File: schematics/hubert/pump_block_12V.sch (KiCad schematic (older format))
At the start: 14 parts, among them M1 PUMP12V, M2 PUMP12V, U2 L6205N

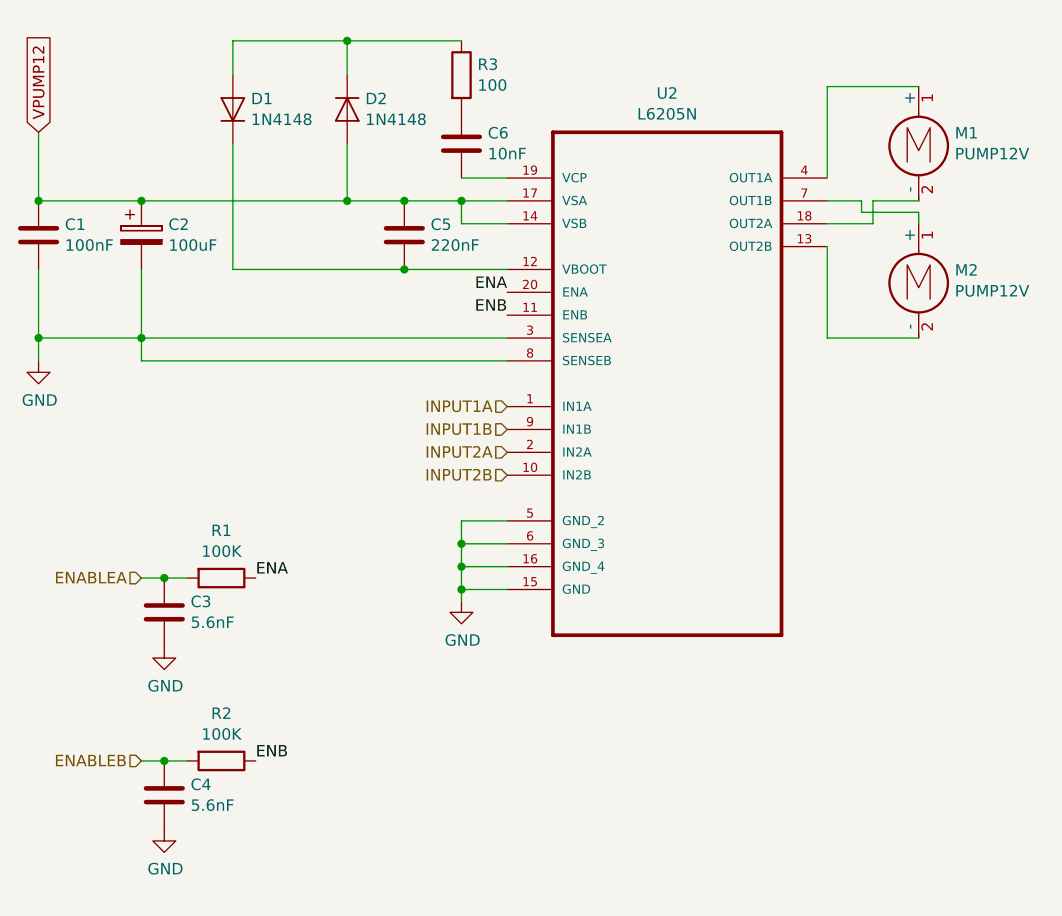
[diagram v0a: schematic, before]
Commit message: updated schematics
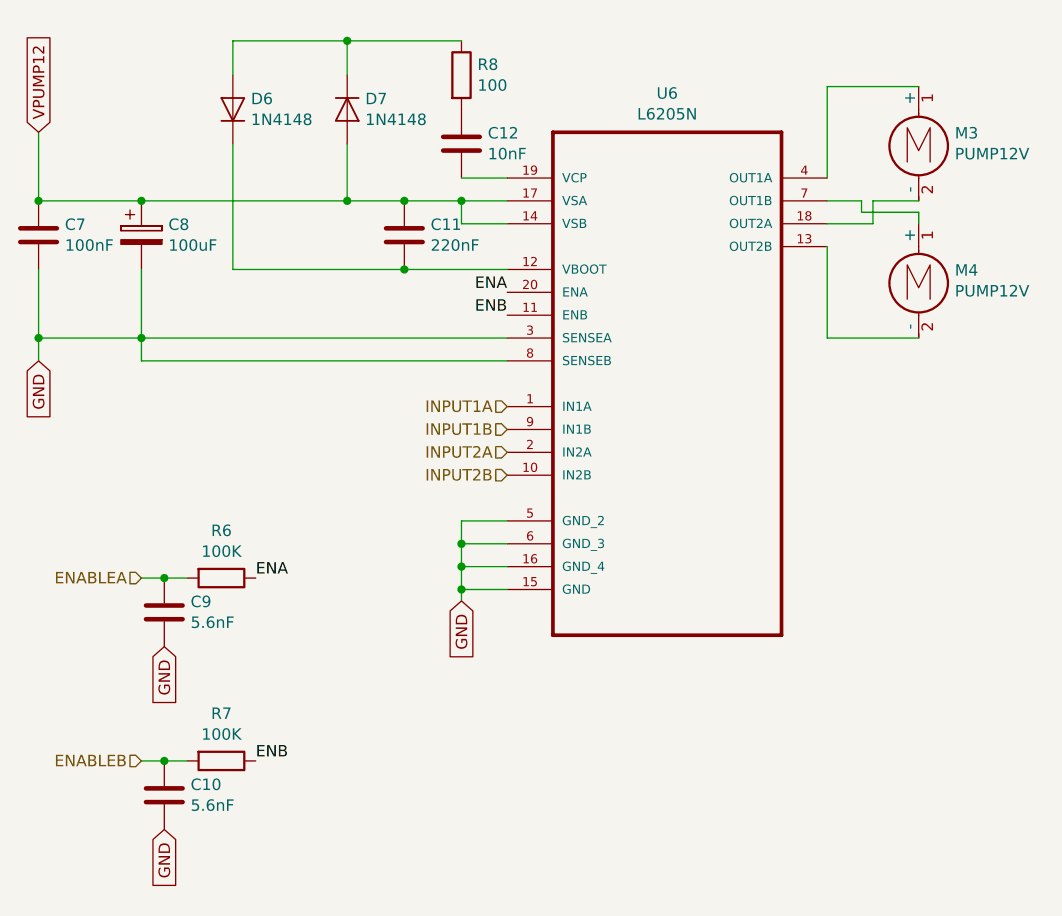
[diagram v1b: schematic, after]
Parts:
- renumbered D1 to D4, D2 to D5, R1 to R3, R2 to R4, R3 to R5, U2 to U5
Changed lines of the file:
@@
 $Descr A4 11693 8268
 encoding utf-8
-Sheet 2 6
+Sheet 3 7
 Title "Hubert"
-Date "2018-10-31"
-Rev "1"
+Date "2018-11-02"
+Rev "1.1"
 Comp ""
 Comment1 ""
@@
 P 6800 3100
 AR Path="/5BDAA834" Ref="U?"  Part="1"
-AR Path="/5BDA8753/5BDAA834" Ref="U2"  Part="1"
-AR Path="/5BDAC3DF/5BDAA834" Ref="U3"  Part="1"
-F 0 "U2" H 6800 4270 50  0000 C CNN
+AR Path="/5BDA8753/5BDAA834" Ref="U5"  Part="1"
+AR Path="/5BDAC3DF/5BDAA834" Ref="U6"  Part="1"
+F 0 "U6" H 6800 4270 50  0000 C CNN
 F 1 "L6205N" H 6800 4179 50  0000 C CNN
 F 2 "DIP254P762X510-20" H 6800 3100 50  0001 L BNN
@@
 	1    0    0    -1
 $EndComp
-$Comp
-L power:GND #PWR?
-U 1 1 5BDAA83B
-P 5900 4150
-AR Path="/5BDAA83B" Ref="#PWR?"  Part="1"
-AR Path="/5BDA8753/5BDAA83B" Ref="#PWR05"  Part="1"
-AR Path="/5BDAC3DF/5BDAA83B" Ref="#PWR010"  Part="1"
-F 0 "#PWR05" H 5900 3900 50  0001 C CNN
-F 1 "GND" H 5905 3977 50  0000 C CNN
-F 2 "" H 5900 4150 50  0001 C CNN
-F 3 "" H 5900 4150 50  0001 C CNN
-	1    5900 4150
-	1    0    0    -1
-$EndComp
 Wire Wire Line
 	5900 4150 5900 4100
@@
 P 5400 2000
 AR Path="/5BDB4D6F" Ref="D?"  Part="1"
-AR Path="/5BDA8753/5BDB4D6F" Ref="D2"  Part="1"
-AR Path="/5BDAC3DF/5BDB4D6F" Ref="D4"  Part="1"
-F 0 "D2" V 5354 2079 50  0000 L CNN
+AR Path="/5BDA8753/5BDB4D6F" Ref="D5"  Part="1"
+AR Path="/5BDAC3DF/5BDB4D6F" Ref="D7"  Part="1"
+F 0 "D7" V 5354 2079 50  0000 L CNN
 F 1 "1N4148" V 5445 2079 50  0000 L CNN
 F 2 "Diode_THT:D_DO-35_SOD27_P7.62mm_Horizontal" H 5400 1825 50  0001 C CNN
@@
 AR Path="/5BDA8753/5BDB4D70" Ref="C6"  Part="1"
 AR Path="/5BDAC3DF/5BDB4D70" Ref="C12"  Part="1"
-F 0 "C6" H 6015 2196 50  0000 L CNN
+F 0 "C12" H 6015 2196 50  0000 L CNN
 F 1 "10nF" H 6015 2105 50  0000 L CNN
 F 2 "" H 5938 2000 50  0001 C CNN
@@
 P 5900 1850
 AR Path="/5BDB4D71" Ref="R?"  Part="1"
-AR Path="/5BDA8753/5BDB4D71" Ref="R3"  Part="1"
-AR Path="/5BDAC3DF/5BDB4D71" Ref="R6"  Part="1"
-F 0 "R3" H 5970 1896 50  0000 L CNN
+AR Path="/5BDA8753/5BDB4D71" Ref="R5"  Part="1"
+AR Path="/5BDAC3DF/5BDB4D71" Ref="R8"  Part="1"
+F 0 "R8" H 5970 1896 50  0000 L CNN
 F 1 "100" H 5970 1805 50  0000 L CNN
 F 2 "" V 5830 1850 50  0001 C CNN
@@
 P 4900 2000
 AR Path="/5BDB4D72" Ref="D?"  Part="1"
-AR Path="/5BDA8753/5BDB4D72" Ref="D1"  Part="1"
-AR Path="/5BDAC3DF/5BDB4D72" Ref="D3"  Part="1"
-F 0 "D1" V 4946 1921 50  0000 R CNN
+AR Path="/5BDA8753/5BDB4D72" Ref="D4"  Part="1"
+AR Path="/5BDAC3DF/5BDB4D72" Ref="D6"  Part="1"
+F 0 "D6" V 4946 1921 50  0000 R CNN
 F 1 "1N4148" V 4855 1921 50  0000 R CNN
 F 2 "Diode_THT:D_DO-35_SOD27_P7.62mm_Horizontal" H 4900 1825 50  0001 C CNN
@@
 AR Path="/5BDA8753/5BDB4D73" Ref="C5"  Part="1"
 AR Path="/5BDAC3DF/5BDB4D73" Ref="C11"  Part="1"
-F 0 "C5" H 5765 2596 50  0000 L CNN
+F 0 "C11" H 5765 2596 50  0000 L CNN
 F 1 "220nF" H 5765 2505 50  0000 L CNN
 F 2 "" H 5688 2400 50  0001 C CNN
@@
 AR Path="/5BDA8753/5BDAA887" Ref="C2"  Part="1"
 AR Path="/5BDAC3DF/5BDAA887" Ref="C8"  Part="1"
-F 0 "C2" H 4618 2596 50  0000 L CNN
+F 0 "C8" H 4618 2596 50  0000 L CNN
 F 1 "100uF" H 4618 2505 50  0000 L CNN
 F 2 "" H 4538 2400 50  0001 C CNN
@@
 AR Path="/5BDA8753/5BDB4D75" Ref="C1"  Part="1"
 AR Path="/5BDAC3DF/5BDB4D75" Ref="C7"  Part="1"
-F 0 "C1" H 4165 2596 50  0000 L CNN
+F 0 "C7" H 4165 2596 50  0000 L CNN
 F 1 "100nF" H 4165 2505 50  0000 L CNN
 F 2 "" H 4088 2400 50  0001 C CNN
@@
 $EndComp
 Connection ~ 4050 2400
-$Comp
-L power:GND #PWR?
-U 1 1 5BDB4D76
-P 4050 3100
-AR Path="/5BDB4D76" Ref="#PWR?"  Part="1"
-AR Path="/5BDA8753/5BDB4D76" Ref="#PWR02"  Part="1"
-AR Path="/5BDAC3DF/5BDB4D76" Ref="#PWR07"  Part="1"
-F 0 "#PWR02" H 4050 2850 50  0001 C CNN
-F 1 "GND" H 4055 2927 50  0000 C CNN
-F 2 "" H 4050 3100 50  0001 C CNN
-F 3 "" H 4050 3100 50  0001 C CNN
-	1    4050 3100
-	1    0    0    -1
-$EndComp
 Wire Wire Line
 	4050 2700 4050 3000
@@
 AR Path="/5BDA8753/5BDAA8AA" Ref="C3"  Part="1"
 AR Path="/5BDAC3DF/5BDAA8AA" Ref="C9"  Part="1"
-F 0 "C3" H 4715 4246 50  0000 L CNN
+F 0 "C9" H 4715 4246 50  0000 L CNN
 F 1 "5.6nF" H 4715 4155 50  0000 L CNN
 F 2 "" H 4638 4050 50  0001 C CNN
@@
 AR Path="/5BDA8753/5BDAA8B1" Ref="C4"  Part="1"
 AR Path="/5BDAC3DF/5BDAA8B1" Ref="C10"  Part="1"
-F 0 "C4" H 4715 5046 50  0000 L CNN
+F 0 "C10" H 4715 5046 50  0000 L CNN
 F 1 "5.6nF" H 4715 4955 50  0000 L CNN
 F 2 "" H 4638 4850 50  0001 C CNN
@@
 $EndComp
 $Comp
-L power:GND #PWR?
-U 1 1 5BDB4D78
-P 4600 4350
-AR Path="/5BDB4D78" Ref="#PWR?"  Part="1"
-AR Path="/5BDA8753/5BDB4D78" Ref="#PWR03"  Part="1"
-AR Path="/5BDAC3DF/5BDB4D78" Ref="#PWR08"  Part="1"
-F 0 "#PWR03" H 4600 4100 50  0001 C CNN
-F 1 "GND" H 4605 4177 50  0000 C CNN
-F 2 "" H 4600 4350 50  0001 C CNN
-F 3 "" H 4600 4350 50  0001 C CNN
-	1    4600 4350
-	1    0    0    -1
-$EndComp
-$Comp
-L power:GND #PWR?
-U 1 1 5BDAA8BE
-P 4600 5150
-AR Path="/5BDAA8BE" Ref="#PWR?"  Part="1"
-AR Path="/5BDA8753/5BDAA8BE" Ref="#PWR04"  Part="1"
-AR Path="/5BDAC3DF/5BDAA8BE" Ref="#PWR09"  Part="1"
-F 0 "#PWR04" H 4600 4900 50  0001 C CNN
-F 1 "GND" H 4605 4977 50  0000 C CNN
-F 2 "" H 4600 5150 50  0001 C CNN
-F 3 "" H 4600 5150 50  0001 C CNN
-	1    4600 5150
-	1    0    0    -1
-$EndComp
-$Comp
 L Device:R R?
 U 1 1 5BDB4D79
 P 4850 4050
 AR Path="/5BDB4D79" Ref="R?"  Part="1"
-AR Path="/5BDA8753/5BDB4D79" Ref="R1"  Part="1"
-AR Path="/5BDAC3DF/5BDB4D79" Ref="R4"  Part="1"
-F 0 "R1" V 4643 4050 50  0000 C CNN
+AR Path="/5BDA8753/5BDB4D79" Ref="R3"  Part="1"
+AR Path="/5BDAC3DF/5BDB4D79" Ref="R6"  Part="1"
+F 0 "R6" V 4643 4050 50  0000 C CNN
 F 1 "100K" V 4734 4050 50  0000 C CNN
 F 2 "" V 4780 4050 50  0001 C CNN
@@
 P 4850 4850
 AR Path="/5BDAA8CB" Ref="R?"  Part="1"
-AR Path="/5BDA8753/5BDAA8CB" Ref="R2"  Part="1"
-AR Path="/5BDAC3DF/5BDAA8CB" Ref="R5"  Part="1"
-F 0 "R2" V 4643 4850 50  0000 C CNN
+AR Path="/5BDA8753/5BDAA8CB" Ref="R4"  Part="1"
+AR Path="/5BDAC3DF/5BDAA8CB" Ref="R7"  Part="1"
+F 0 "R7" V 4643 4850 50  0000 C CNN
 F 1 "100K" V 4734 4850 50  0000 C CNN
 F 2 "" V 4780 4850 50  0001 C CNN
@@
 AR Path="/5BDA8753/5BDB4D7A" Ref="M1"  Part="1"
 AR Path="/5BDAC3DF/5BDB4D7A" Ref="M3"  Part="1"
-F 0 "M1" H 8058 2096 50  0000 L CNN
+F 0 "M3" H 8058 2096 50  0000 L CNN
 F 1 "PUMP12V" H 8058 2005 50  0000 L CNN
 F 2 "" H 7900 2010 50  0001 C CNN
@@
 AR Path="/5BDA8753/5BDAA8E9" Ref="M2"  Part="1"
 AR Path="/5BDAC3DF/5BDAA8E9" Ref="M4"  Part="1"
-F 0 "M2" H 8058 2696 50  0000 L CNN
+F 0 "M4" H 8058 2696 50  0000 L CNN
 F 1 "PUMP12V" H 8058 2605 50  0000 L CNN
 F 2 "" H 7900 2610 50  0001 C CNN
@@
 Text GLabel 4050 2100 1    50   Input ~ 0
 VPUMP12
+Text GLabel 4600 4350 3    50   Input ~ 0
+GND
+Text GLabel 4600 5150 3    50   Input ~ 0
+GND
+Text GLabel 4050 3100 3    50   Input ~ 0
+GND
+Text GLabel 5900 4150 3    50   Input ~ 0
+GND
 $EndSCHEMATC

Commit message: started working on layout
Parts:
- C1, C3, C4, C5, C6: footprint (none) -> Capacitor_THT:CP_Radial_D5.0mm_P2.50mm
- C2: footprint (none) -> Capacitor_THT:CP_Radial_D6.3mm_P2.50mm
- R3, R4, R5: footprint (none) -> Resistor_THT:R_Axial_DIN0617_L17.0mm_D6.0mm_P25.40mm_Horizontal
- U5: footprint DIP254P762X510-20 -> Package_DIP:DIP-20_W7.62mm_Socket
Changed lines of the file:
@@
 Sheet 3 7
 Title "Hubert"
-Date "2018-11-02"
-Rev "1.1"
+Date "2018-11-05"
+Rev "1.2"
 Comp ""
 Comment1 ""
@@
 AR Path="/5BDA8753/5BDAA834" Ref="U5"  Part="1"
 AR Path="/5BDAC3DF/5BDAA834" Ref="U6"  Part="1"
-F 0 "U6" H 6800 4270 50  0000 C CNN
+F 0 "U5" H 6800 4270 50  0000 C CNN
 F 1 "L6205N" H 6800 4179 50  0000 C CNN
-F 2 "DIP254P762X510-20" H 6800 3100 50  0001 L BNN
+F 2 "Package_DIP:DIP-20_W7.62mm_Socket" H 6800 3100 50  0001 L BNN
 F 3 "L6205N" H 6800 3100 50  0001 L BNN
 F 4 "Unavailable" H 6800 3100 50  0001 L BNN "Field4"
@@
 AR Path="/5BDA8753/5BDB4D6F" Ref="D5"  Part="1"
 AR Path="/5BDAC3DF/5BDB4D6F" Ref="D7"  Part="1"
-F 0 "D7" V 5354 2079 50  0000 L CNN
+F 0 "D5" V 5354 2079 50  0000 L CNN
 F 1 "1N4148" V 5445 2079 50  0000 L CNN
 F 2 "Diode_THT:D_DO-35_SOD27_P7.62mm_Horizontal" H 5400 1825 50  0001 C CNN
@@
 AR Path="/5BDA8753/5BDB4D70" Ref="C6"  Part="1"
 AR Path="/5BDAC3DF/5BDB4D70" Ref="C12"  Part="1"
-F 0 "C12" H 6015 2196 50  0000 L CNN
+F 0 "C6" H 6015 2196 50  0000 L CNN
 F 1 "10nF" H 6015 2105 50  0000 L CNN
-F 2 "" H 5938 2000 50  0001 C CNN
+F 2 "Capacitor_THT:CP_Radial_D5.0mm_P2.50mm" H 5938 2000 50  0001 C CNN
 F 3 "~" H 5900 2150 50  0001 C CNN
 	1    5900 2150
@@
 AR Path="/5BDA8753/5BDB4D71" Ref="R5"  Part="1"
 AR Path="/5BDAC3DF/5BDB4D71" Ref="R8"  Part="1"
-F 0 "R8" H 5970 1896 50  0000 L CNN
+F 0 "R5" H 5970 1896 50  0000 L CNN
 F 1 "100" H 5970 1805 50  0000 L CNN
-F 2 "" V 5830 1850 50  0001 C CNN
+F 2 "Resistor_THT:R_Axial_DIN0617_L17.0mm_D6.0mm_P25.40mm_Horizontal" V 5830 1850 50  0001 C CNN
 F 3 "~" H 5900 1850 50  0001 C CNN
 	1    5900 1850
@@
 AR Path="/5BDA8753/5BDB4D72" Ref="D4"  Part="1"
 AR Path="/5BDAC3DF/5BDB4D72" Ref="D6"  Part="1"
-F 0 "D6" V 4946 1921 50  0000 R CNN
+F 0 "D4" V 4946 1921 50  0000 R CNN
 F 1 "1N4148" V 4855 1921 50  0000 R CNN
 F 2 "Diode_THT:D_DO-35_SOD27_P7.62mm_Horizontal" H 4900 1825 50  0001 C CNN
@@
 AR Path="/5BDA8753/5BDB4D73" Ref="C5"  Part="1"
 AR Path="/5BDAC3DF/5BDB4D73" Ref="C11"  Part="1"
-F 0 "C11" H 5765 2596 50  0000 L CNN
+F 0 "C5" H 5765 2596 50  0000 L CNN
 F 1 "220nF" H 5765 2505 50  0000 L CNN
-F 2 "" H 5688 2400 50  0001 C CNN
+F 2 "Capacitor_THT:CP_Radial_D5.0mm_P2.50mm" H 5688 2400 50  0001 C CNN
 F 3 "~" H 5650 2550 50  0001 C CNN
 	1    5650 2550
@@
 AR Path="/5BDA8753/5BDAA887" Ref="C2"  Part="1"
 AR Path="/5BDAC3DF/5BDAA887" Ref="C8"  Part="1"
-F 0 "C8" H 4618 2596 50  0000 L CNN
+F 0 "C2" H 4618 2596 50  0000 L CNN
 F 1 "100uF" H 4618 2505 50  0000 L CNN
-F 2 "" H 4538 2400 50  0001 C CNN
+F 2 "Capacitor_THT:CP_Radial_D6.3mm_P2.50mm" H 4538 2400 50  0001 C CNN
 F 3 "~" H 4500 2550 50  0001 C CNN
 	1    4500 2550
@@
 AR Path="/5BDA8753/5BDB4D75" Ref="C1"  Part="1"
 AR Path="/5BDAC3DF/5BDB4D75" Ref="C7"  Part="1"
-F 0 "C7" H 4165 2596 50  0000 L CNN
+F 0 "C1" H 4165 2596 50  0000 L CNN
 F 1 "100nF" H 4165 2505 50  0000 L CNN
-F 2 "" H 4088 2400 50  0001 C CNN
+F 2 "Capacitor_THT:CP_Radial_D5.0mm_P2.50mm" H 4088 2400 50  0001 C CNN
 F 3 "~" H 4050 2550 50  0001 C CNN
 	1    4050 2550
@@
 AR Path="/5BDA8753/5BDAA8AA" Ref="C3"  Part="1"
 AR Path="/5BDAC3DF/5BDAA8AA" Ref="C9"  Part="1"
-F 0 "C9" H 4715 4246 50  0000 L CNN
+F 0 "C3" H 4715 4246 50  0000 L CNN
 F 1 "5.6nF" H 4715 4155 50  0000 L CNN
-F 2 "" H 4638 4050 50  0001 C CNN
+F 2 "Capacitor_THT:CP_Radial_D5.0mm_P2.50mm" H 4638 4050 50  0001 C CNN
 F 3 "~" H 4600 4200 50  0001 C CNN
 	1    4600 4200
@@
 AR Path="/5BDA8753/5BDAA8B1" Ref="C4"  Part="1"
 AR Path="/5BDAC3DF/5BDAA8B1" Ref="C10"  Part="1"
-F 0 "C10" H 4715 5046 50  0000 L CNN
+F 0 "C4" H 4715 5046 50  0000 L CNN
 F 1 "5.6nF" H 4715 4955 50  0000 L CNN
-F 2 "" H 4638 4850 50  0001 C CNN
+F 2 "Capacitor_THT:CP_Radial_D5.0mm_P2.50mm" H 4638 4850 50  0001 C CNN
 F 3 "~" H 4600 5000 50  0001 C CNN
 	1    4600 5000
@@
 AR Path="/5BDA8753/5BDB4D79" Ref="R3"  Part="1"
 AR Path="/5BDAC3DF/5BDB4D79" Ref="R6"  Part="1"
-F 0 "R6" V 4643 4050 50  0000 C CNN
+F 0 "R3" V 4643 4050 50  0000 C CNN
 F 1 "100K" V 4734 4050 50  0000 C CNN
-F 2 "" V 4780 4050 50  0001 C CNN
+F 2 "Resistor_THT:R_Axial_DIN0617_L17.0mm_D6.0mm_P25.40mm_Horizontal" V 4780 4050 50  0001 C CNN
 F 3 "~" H 4850 4050 50  0001 C CNN
 	1    4850 4050
@@
 AR Path="/5BDA8753/5BDAA8CB" Ref="R4"  Part="1"
 AR Path="/5BDAC3DF/5BDAA8CB" Ref="R7"  Part="1"
-F 0 "R7" V 4643 4850 50  0000 C CNN
+F 0 "R4" V 4643 4850 50  0000 C CNN
 F 1 "100K" V 4734 4850 50  0000 C CNN
-F 2 "" V 4780 4850 50  0001 C CNN
+F 2 "Resistor_THT:R_Axial_DIN0617_L17.0mm_D6.0mm_P25.40mm_Horizontal" V 4780 4850 50  0001 C CNN
 F 3 "~" H 4850 4850 50  0001 C CNN
 	1    4850 4850
@@
 AR Path="/5BDA8753/5BDB4D7A" Ref="M1"  Part="1"
 AR Path="/5BDAC3DF/5BDB4D7A" Ref="M3"  Part="1"
-F 0 "M3" H 8058 2096 50  0000 L CNN
+F 0 "M1" H 8058 2096 50  0000 L CNN
 F 1 "PUMP12V" H 8058 2005 50  0000 L CNN
 F 2 "" H 7900 2010 50  0001 C CNN
@@
 AR Path="/5BDA8753/5BDAA8E9" Ref="M2"  Part="1"
 AR Path="/5BDAC3DF/5BDAA8E9" Ref="M4"  Part="1"
-F 0 "M4" H 8058 2696 50  0000 L CNN
+F 0 "M2" H 8058 2696 50  0000 L CNN
 F 1 "PUMP12V" H 8058 2605 50  0000 L CNN
 F 2 "" H 7900 2610 50  0001 C CNN
